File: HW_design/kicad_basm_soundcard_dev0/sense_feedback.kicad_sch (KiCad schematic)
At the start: 14 parts, among them U301 LSM6DSL, U401 ICP20100

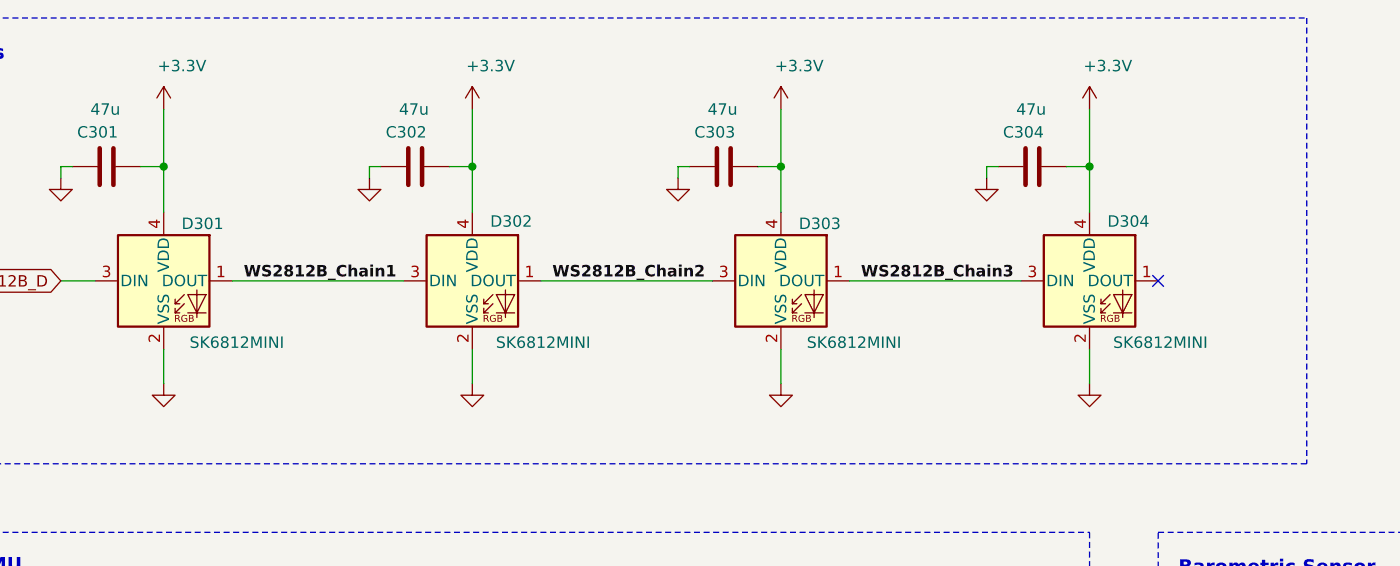
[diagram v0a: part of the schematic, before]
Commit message: Changed Footprints for LED RGB, SD, AudioJack, USB
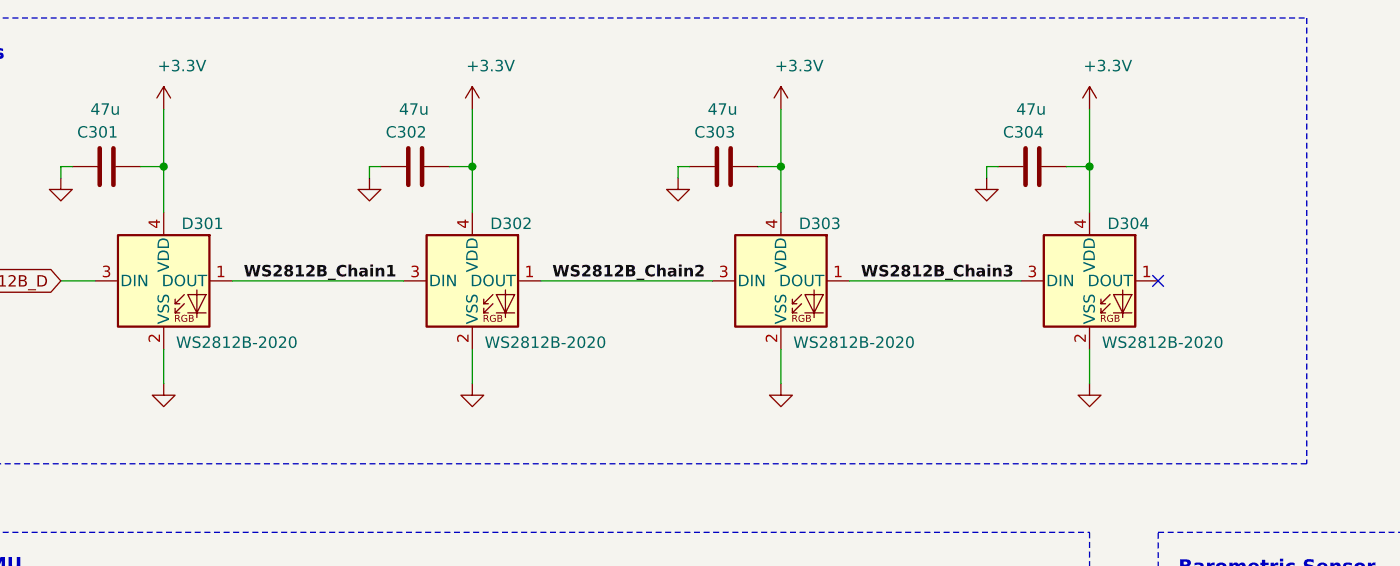
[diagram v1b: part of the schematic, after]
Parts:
- D301, D302, D303, D304: value SK6812MINI -> WS2812B-2020; footprint LED_SMD:LED_SK6812MINI_PLCC4_3.5x3.5mm_P1.75mm -> LED_SMD:LED_WS2812B-2020_PLCC4_2.0x2.0mm
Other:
- company: (none) -> BUCHAREST APPLIED STEAM MUSEUM
- title: (none) -> BASM SOUNDCARD
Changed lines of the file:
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@@
 	(generator_version "8.0")
 	(paper "A4")
+	(title_block
+		(title "BASM SOUNDCARD")
+		(rev "1")
+		(company "BUCHAREST APPLIED STEAM MUSEUM")
+		(comment 1 "Updated RGB LED P/N to WS2812B-2020")
+	)
 	(junction
 		(at 97.79 45.72)
@@
 	)
 	(symbol
+		(lib_id "LED:SK6812MINI")
+		(at 97.79 58.42 0)
+		(unit 1)
+		(exclude_from_sim no)
+		(in_bom yes)
+		(on_board yes)
+		(dnp no)
+		(property "Reference" "D302"
+			(at 102.108 52.07 0)
+			(effects
+				(font
+					(size 1.27 1.27)
+				)
+			)
+		)
+		(property "Value" "WS2812B-2020"
+			(at 105.918 65.278 0)
+			(effects
+				(font
+					(size 1.27 1.27)
+				)
+			)
+		)
+		(property "Footprint" "LED_SMD:LED_WS2812B-2020_PLCC4_2.0x2.0mm"
+			(at 99.06 66.04 0)
+			(effects
+				(font
+					(size 1.27 1.27)
+				)
+				(justify left top)
+				(hide yes)
+			)
+		)
+		(property "Datasheet" "https://cdn-shop.adafruit.com/product-files/2686/SK6812MINI_REV.01-1-2.pdf"
+			(at 100.33 67.945 0)
+			(effects
+				(font
+					(size 1.27 1.27)
+				)
+				(justify left top)
+				(hide yes)
+			)
+		)
+		(property "Description" "RGB LED with integrated controller"
+			(at 97.79 58.42 0)
+			(effects
+				(font
+					(size 1.27 1.27)
+				)
+				(hide yes)
+			)
+		)
+		(pin "2"
+		)
+		(pin "3"
+		)
+		(pin "4"
+		)
+		(pin "1"
+		)
+		(instances
+			(project "basmsoundcard"
+				(path "/a2ae8555-7422-4c55-bf44-8cc769543ba0/56e71c46-1e9f-4234-b489-780fdafeb799"
+					(reference "D302")
+					(unit 1)
+				)
+			)
+		)
+	)
+	(symbol
 		(lib_id "Device:C")
 		(at 260.35 109.22 270)
@@
 	)
 	(symbol
+		(lib_id "LED:SK6812MINI")
+		(at 166.37 58.42 0)
+		(unit 1)
+		(exclude_from_sim no)
+		(in_bom yes)
+		(on_board yes)
+		(dnp no)
+		(property "Reference" "D304"
+			(at 170.688 52.07 0)
+			(effects
+				(font
+					(size 1.27 1.27)
+				)
+			)
+		)
+		(property "Value" "WS2812B-2020"
+			(at 174.498 65.278 0)
+			(effects
+				(font
+					(size 1.27 1.27)
+				)
+			)
+		)
+		(property "Footprint" "LED_SMD:LED_WS2812B-2020_PLCC4_2.0x2.0mm"
+			(at 167.64 66.04 0)
+			(effects
+				(font
+					(size 1.27 1.27)
+				)
+				(justify left top)
+				(hide yes)
+			)
+		)
+		(property "Datasheet" "https://cdn-shop.adafruit.com/product-files/2686/SK6812MINI_REV.01-1-2.pdf"
+			(at 168.91 67.945 0)
+			(effects
+				(font
+					(size 1.27 1.27)
+				)
+				(justify left top)
+				(hide yes)
+			)
+		)
+		(property "Description" "RGB LED with integrated controller"
+			(at 166.37 58.42 0)
+			(effects
+				(font
+					(size 1.27 1.27)
+				)
+				(hide yes)
+			)
+		)
+		(pin "2"
+		)
+		(pin "3"
+		)
+		(pin "4"
+		)
+		(pin "1"
+		)
+		(instances
+			(project "basmsoundcard"
+				(path "/a2ae8555-7422-4c55-bf44-8cc769543ba0/56e71c46-1e9f-4234-b489-780fdafeb799"
+					(reference "D304")
+					(unit 1)
+				)
+			)
+		)
+	)
+	(symbol
 		(lib_id "power:GND")
 		(at 120.65 46.99 0)
@@
 	)
 	(symbol
-		(lib_id "LED:SK6812MINI")
-		(at 132.08 58.42 0)
-		(unit 1)
-		(exclude_from_sim no)
-		(in_bom yes)
-		(on_board yes)
-		(dnp no)
-		(property "Reference" "D303"
-			(at 136.398 52.07 0)
-			(effects
-				(font
-					(size 1.27 1.27)
-				)
-			)
-		)
-		(property "Value" "SK6812MINI"
-			(at 140.208 65.278 0)
-			(effects
-				(font
-					(size 1.27 1.27)
-				)
-			)
-		)
-		(property "Footprint" "LED_SMD:LED_SK6812MINI_PLCC4_3.5x3.5mm_P1.75mm"
-			(at 133.35 66.04 0)
-			(effects
-				(font
-					(size 1.27 1.27)
-				)
-				(justify left top)
-				(hide yes)
-			)
-		)
-		(property "Datasheet" "https://cdn-shop.adafruit.com/product-files/2686/SK6812MINI_REV.01-1-2.pdf"
-			(at 134.62 67.945 0)
-			(effects
-				(font
-					(size 1.27 1.27)
-				)
-				(justify left top)
-				(hide yes)
-			)
-		)
-		(property "Description" "RGB LED with integrated controller"
-			(at 132.08 58.42 0)
-			(effects
-				(font
-					(size 1.27 1.27)
-				)
-				(hide yes)
-			)
-		)
-		(pin "2"
-		)
-		(pin "3"
-		)
-		(pin "4"
-		)
-		(pin "1"
-		)
-		(instances
-			(project "basmsoundcard"
-				(path "/a2ae8555-7422-4c55-bf44-8cc769543ba0/56e71c46-1e9f-4234-b489-780fdafeb799"
-					(reference "D303")
-					(unit 1)
-				)
-			)
-		)
-	)
-	(symbol
 		(lib_id "power:GND")
 		(at 269.24 130.81 0)
@@
 			)
 		)
-		(property "Value" "SK6812MINI"
+		(property "Value" "WS2812B-2020"
 			(at 71.628 65.278 0)
 			(effects
@@
 			)
 		)
-		(property "Footprint" "LED_SMD:LED_SK6812MINI_PLCC4_3.5x3.5mm_P1.75mm"
+		(property "Footprint" "LED_SMD:LED_WS2812B-2020_PLCC4_2.0x2.0mm"
 			(at 64.77 66.04 0)
 			(effects
@@
 	(symbol
 		(lib_id "LED:SK6812MINI")
-		(at 166.37 58.42 0)
+		(at 132.08 58.42 0)
 		(unit 1)
 		(exclude_from_sim no)
@@
 		(on_board yes)
 		(dnp no)
-		(property "Reference" "D304"
-			(at 170.688 51.816 0)
-			(effects
-				(font
-					(size 1.27 1.27)
-				)
-			)
-		)
-		(property "Value" "SK6812MINI"
-			(at 174.244 65.278 0)
-			(effects
-				(font
-					(size 1.27 1.27)
-				)
-			)
-		)
-		(property "Footprint" "LED_SMD:LED_SK6812MINI_PLCC4_3.5x3.5mm_P1.75mm"
-			(at 167.64 66.04 0)
+		(property "Reference" "D303"
+			(at 136.398 52.07 0)
+			(effects
+				(font
+					(size 1.27 1.27)
+				)
+			)
+		)
+		(property "Value" "WS2812B-2020"
+			(at 140.208 65.278 0)
+			(effects
+				(font
+					(size 1.27 1.27)
+				)
+			)
+		)
+		(property "Footprint" "LED_SMD:LED_WS2812B-2020_PLCC4_2.0x2.0mm"
+			(at 133.35 66.04 0)
 			(effects
 				(font
@@
 		)
 		(property "Datasheet" "https://cdn-shop.adafruit.com/product-files/2686/SK6812MINI_REV.01-1-2.pdf"
-			(at 168.91 67.945 0)
+			(at 134.62 67.945 0)
 			(effects
 				(font
@@
 		)
 		(property "Description" "RGB LED with integrated controller"
-			(at 166.37 58.42 0)
+			(at 132.08 58.42 0)
 			(effects
 				(font
@@
 			(project "basmsoundcard"
 				(path "/a2ae8555-7422-4c55-bf44-8cc769543ba0/56e71c46-1e9f-4234-b489-780fdafeb799"
-					(reference "D304")
+					(reference "D303")
 					(unit 1)
 				)
@@
 					(unit 1)
 				)
-			)
-		)
-	)
-	(symbol
-		(lib_id "LED:SK6812MINI")
-		(at 97.79 58.42 0)
-		(unit 1)
-		(exclude_from_sim no)
-		(in_bom yes)
-		(on_board yes)
-		(dnp no)
-		(property "Reference" "D302"
-			(at 102.108 51.816 0)
-			(effects
-				(font
-					(size 1.27 1.27)
-				)
-			)
-		)
-		(property "Value" "SK6812MINI"
-			(at 105.664 65.278 0)
-			(effects
-				(font
-					(size 1.27 1.27)
-				)
-			)
-		)
-		(property "Footprint" "LED_SMD:LED_SK6812MINI_PLCC4_3.5x3.5mm_P1.75mm"
-			(at 99.06 66.04 0)
-			(effects
-				(font
-					(size 1.27 1.27)
-				)
-				(justify left top)
-				(hide yes)
-			)
-		)
-		(property "Datasheet" "https://cdn-shop.adafruit.com/product-files/2686/SK6812MINI_REV.01-1-2.pdf"
-			(at 100.33 67.945 0)
-			(effects
-				(font
-					(size 1.27 1.27)
-				)
-				(justify left top)
-				(hide yes)
-			)
-		)
-		(property "Description" "RGB LED with integrated controller"
-			(at 97.79 58.42 0)
-			(effects
-				(font
-					(size 1.27 1.27)
-				)
-				(hide yes)
-			)
-		)
-		(pin "2"
-		)
-		(pin "3"
-		)
-		(pin "4"
-		)
-		(pin "1"
-		)
-		(instances
-			(project "basmsoundcard"
-				(path "/a2ae8555-7422-4c55-bf44-8cc769543ba0/56e71c46-1e9f-4234-b489-780fdafeb799"
-					(reference "D302")
-					(unit 1)
-				)
